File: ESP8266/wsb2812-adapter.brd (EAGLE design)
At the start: 9.5 x 11.4 mm, 4 parts, among them CON1 USBMICRO-NO_CENTER

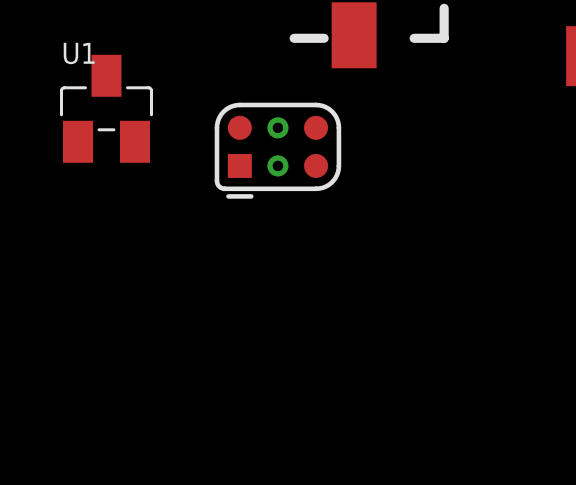
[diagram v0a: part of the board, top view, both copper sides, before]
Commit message: added power supply
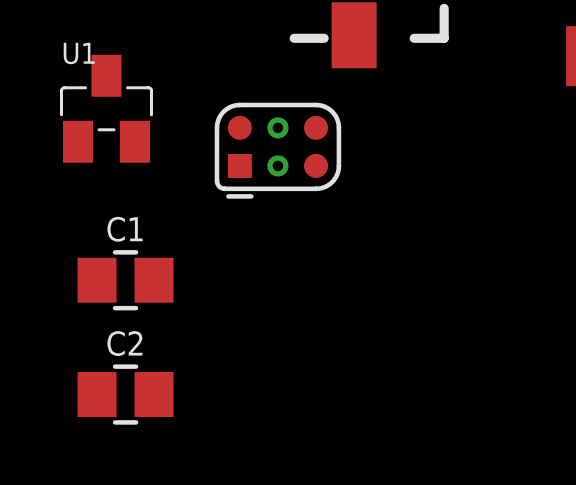
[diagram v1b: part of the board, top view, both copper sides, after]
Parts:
- added C1, C2: 1uF, p.peter-rcl:C0805
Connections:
- removed net VCC: CON-1.P$2
- new net +3V3: C2.1, CON-1.P$2, U$1.P$8, U1.P$2
- new net +5V: C1.1, CON1.VUSB, U1.P$3
- new net N$2: CON-1.P$3
- new net RX: CON-1.P$1, U$1.P$4
- new net SEL: U$1.P$6
- new net TX: CON-1.P$4, U$1.P$3
- net GND: now also C1.2, C2.2, CON1.GND, U$1.P$1, U1.P$1
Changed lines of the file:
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@@
 <?xml version="1.0" encoding="utf-8"?>
 <!DOCTYPE eagle SYSTEM "eagle.dtd">
-<eagle version="7.3.0">
+<eagle version="7.1.0">
 <drawing>
 <settings>
@@
 <element name="CON-1" library="p.peter-connectors" package="POGO-1.27-6_PIN-MADWORM" value="" x="-2.54" y="-16.51"/>
 <element name="U1" library="p.peter-regulators" package="SOT23" value="" x="-8.255" y="-15.24"/>
+<element name="C1" library="p.peter-rcl" package="C0805" value="1uF" x="-7.62" y="-20.955"/>
+<element name="C2" library="p.peter-rcl" package="C0805" value="1uF" x="-7.62" y="-24.765"/>
 </elements>
 <signals>
 <signal name="GND">
+<contactref element="U1" pad="P$1"/>
+<contactref element="C1" pad="2"/>
+<contactref element="C2" pad="2"/>
+<contactref element="CON1" pad="GND"/>
+<contactref element="U$1" pad="P$1"/>
 <contactref element="CON-1" pad="P$6"/>
-</signal>
-<signal name="VCC">
+<wire x1="-6.67" y1="-20.955" x2="-6.67" y2="-24.765" width="0" layer="19" extent="1-1"/>
+<wire x1="-9.205" y1="-16.34" x2="-6.67" y2="-20.955" width="0" layer="19" extent="1-1"/>
+<wire x1="-1.27" y1="-15.875" x2="-6.67" y2="-20.955" width="0" layer="19" extent="1-1"/>
+<wire x1="2.7" y1="-10.19" x2="-1.27" y2="-15.875" width="0" layer="19" extent="1-1"/>
+<wire x1="19.7" y1="-0.485" x2="2.7" y2="-10.19" width="0" layer="19" extent="1-1"/>
+</signal>
+<signal name="+5V">
+<contactref element="U1" pad="P$3"/>
+<contactref element="C1" pad="1"/>
+<contactref element="CON1" pad="VUSB"/>
+<wire x1="-8.255" y1="-14.14" x2="-8.57" y2="-20.955" width="0" layer="19" extent="1-1"/>
+<wire x1="2.7" y1="-7.59" x2="-8.255" y2="-14.14" width="0" layer="19" extent="1-1"/>
+</signal>
+<signal name="+3V3">
+<contactref element="U1" pad="P$2"/>
+<contactref element="C2" pad="1"/>
+<contactref element="U$1" pad="P$8"/>
 <contactref element="CON-1" pad="P$2"/>
+<wire x1="-7.305" y1="-16.34" x2="-8.57" y2="-24.765" width="0" layer="19" extent="1-1"/>
+<wire x1="-3.81" y1="-15.875" x2="-7.305" y2="-16.34" width="0" layer="19" extent="1-1"/>
+<wire x1="7.7" y1="-13.485" x2="-3.81" y2="-15.875" width="0" layer="19" extent="1-1"/>
+</signal>
+<signal name="SEL">
+<contactref element="U$1" pad="P$6"/>
+</signal>
+<signal name="RX">
+<contactref element="U$1" pad="P$4"/>
+<contactref element="CON-1" pad="P$1"/>
+<wire x1="13.7" y1="-0.485" x2="-3.81" y2="-17.145" width="0" layer="19" extent="1-1"/>
+</signal>
+<signal name="TX">
+<contactref element="U$1" pad="P$3"/>
+<contactref element="CON-1" pad="P$4"/>
+<wire x1="15.7" y1="-0.485" x2="-2.54" y2="-15.875" width="0" layer="19" extent="1-1"/>
+</signal>
+<signal name="N$2">
+<contactref element="CON-1" pad="P$3"/>
 </signal>
 </signals>

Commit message: V0.1 done
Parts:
- added +5V, GND: PTR1PAD1-20, testpad:P1-20
- added DAT: (no value), pinhead:1X01
- added R1, R2, R3: 10k, p.peter-rcl:R0603
- added U$3: (no value), p.peter-doc:LOGO-JUSTGEEK-XS
- moved CON-1 33.7 mm to (20.3, 8.26), flipped to the bottom, turned to 270 degrees
- moved C1 33.6 mm to (8.89, 8.26), turned to 180 degrees
- moved C2 31.4 mm to (8.89, 1.91), turned to 180 degrees
- moved U1 26.6 mm to (8.89, 5.08)
- moved CON1 17.3 mm to (3.30, 8.26)
- moved U$1 17.0 mm to (20.3, 8.26), turned to 180 degrees
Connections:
- removed net SEL: U$1.P$6
- new net FLASH: CON-1.P$3, U$1.P$14
- new net N$1: R1.1, U$1.P$12
- new net N$3: R2.1, U$1.P$13
- new net RESET: CON-1.P$5, R3.1, U$1.P$6
- net +3V3: now also R2.2, R3.2
- net +5V: now also +5V.TP
- net GND: now also GND.TP, R1.2
- net N$2: now also DAT.1, U$1.P$10; no longer CON-1.P$3
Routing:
- net GND: track 0.00 -> 72.1 mm, vias 0 -> 2
- net +3V3: track 0.00 -> 55.6 mm, vias 0 -> 4
- net +5V: track 0.00 -> 38.4 mm, vias 0 -> 1
- net RESET: track 0.00 -> 26.9 mm, vias 0 -> 3
- net N$2: track 0.00 -> 15.7 mm, vias 0 -> 1
- net N$1: track 0.00 -> 15.2 mm
- net FLASH: track 0.00 -> 14.9 mm, vias 0 -> 2
- net RX: track 0.00 -> 11.8 mm, vias 0 -> 1
- net TX: track 0.00 -> 11.4 mm, vias 0 -> 1
- net N$3: track 0.00 -> 10.2 mm
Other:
- board size 9.5 x 11.4 mm -> 34.3 x 16.5 mm
- board text added: "+5V"
- board text added: "DAT"
- board text added: "ESP-WS2812 ADAPTER"
- board text added: "FL"
- board text added: "GND"
- board text added: "RES"
- board text added: "RX"
- board text added: "TX"
- board text added: "V+"
- board text added: "justgeek.de"
- board text added: "v0.1"
